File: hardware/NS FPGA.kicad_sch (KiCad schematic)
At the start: 0 parts

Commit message: Update KiCad schematics and add gowin_fpga symbol library
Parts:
- added U1: ~, Gowin FPGA:BGA-64_8x8_4.2x4.2mm, symbol Gowin FPGA:GW1NSR-4C_MG64P

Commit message: Update schematic
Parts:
- added J1: USB_C_Receptacle_USB2.0_14P, symbol Connector:USB_C_Receptacle_USB2.0_14P
- added J2, J3: Conn_01x24_Pin, symbol Connector:Conn_01x24_Pin
- added J4: Conn_01x06_Pin, symbol Connector:Conn_01x06_Pin
- added SW1: SW_Push, symbol Switch:SW_Push
- added U2: CP2102N-Axx-xQFN24, Package_DFN_QFN:QFN-24-1EP_4x4mm_P0.5mm_EP2.6x2.6mm, symbol Interface_USB:CP2102N-Axx-xQFN24
- added U3: AP2112K-3.3, Package_TO_SOT_SMD:SOT-23-5, symbol Regulator_Linear:AP2112K-3.3
- added U4: AP2112K-1.2, Package_TO_SOT_SMD:SOT-23-5, symbol Regulator_Linear:AP2112K-1.2
- added Y1: SG-8002CE, Oscillator:Oscillator_SMD_SeikoEpson_SG8002CE-4Pin_3.2x2.5mm, symbol Oscillator:SG-8002CE
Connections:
- new net: J1.A1 (GND), J1.A12 (GND), J1.B1 (GND), J1.B12 (GND)
- new net: J1.A4 (VBUS), J1.A9 (VBUS), J1.B4 (VBUS), J1.B9 (VBUS)
- new net: U2.2 (GND), U2.25 (GND)

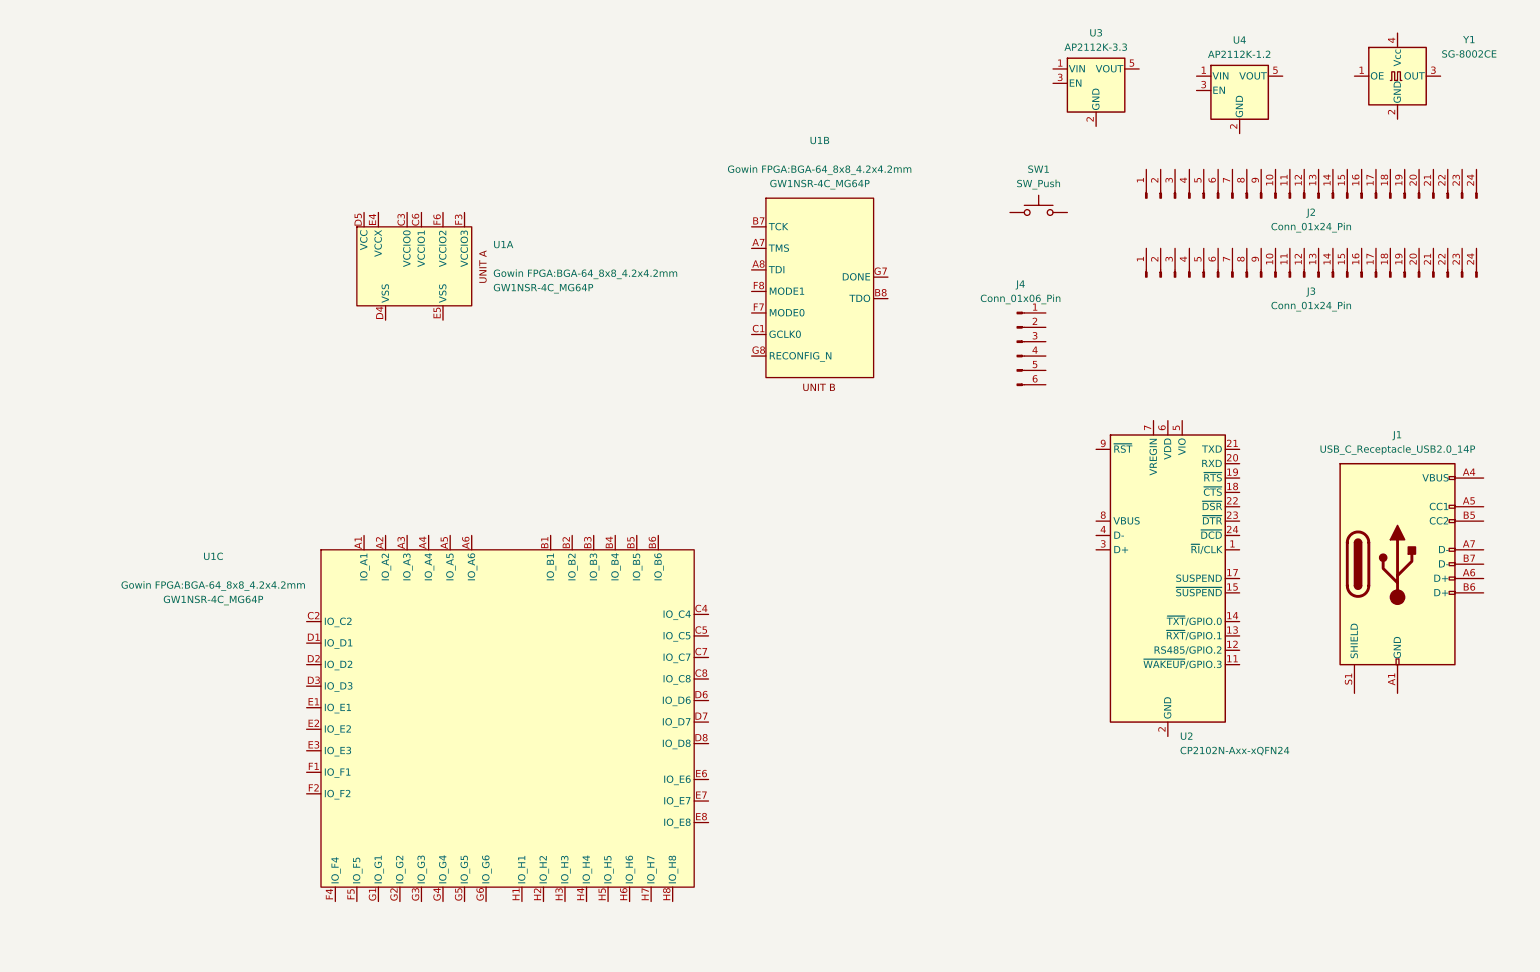
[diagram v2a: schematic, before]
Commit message: drawn 80% of the circuit schematic
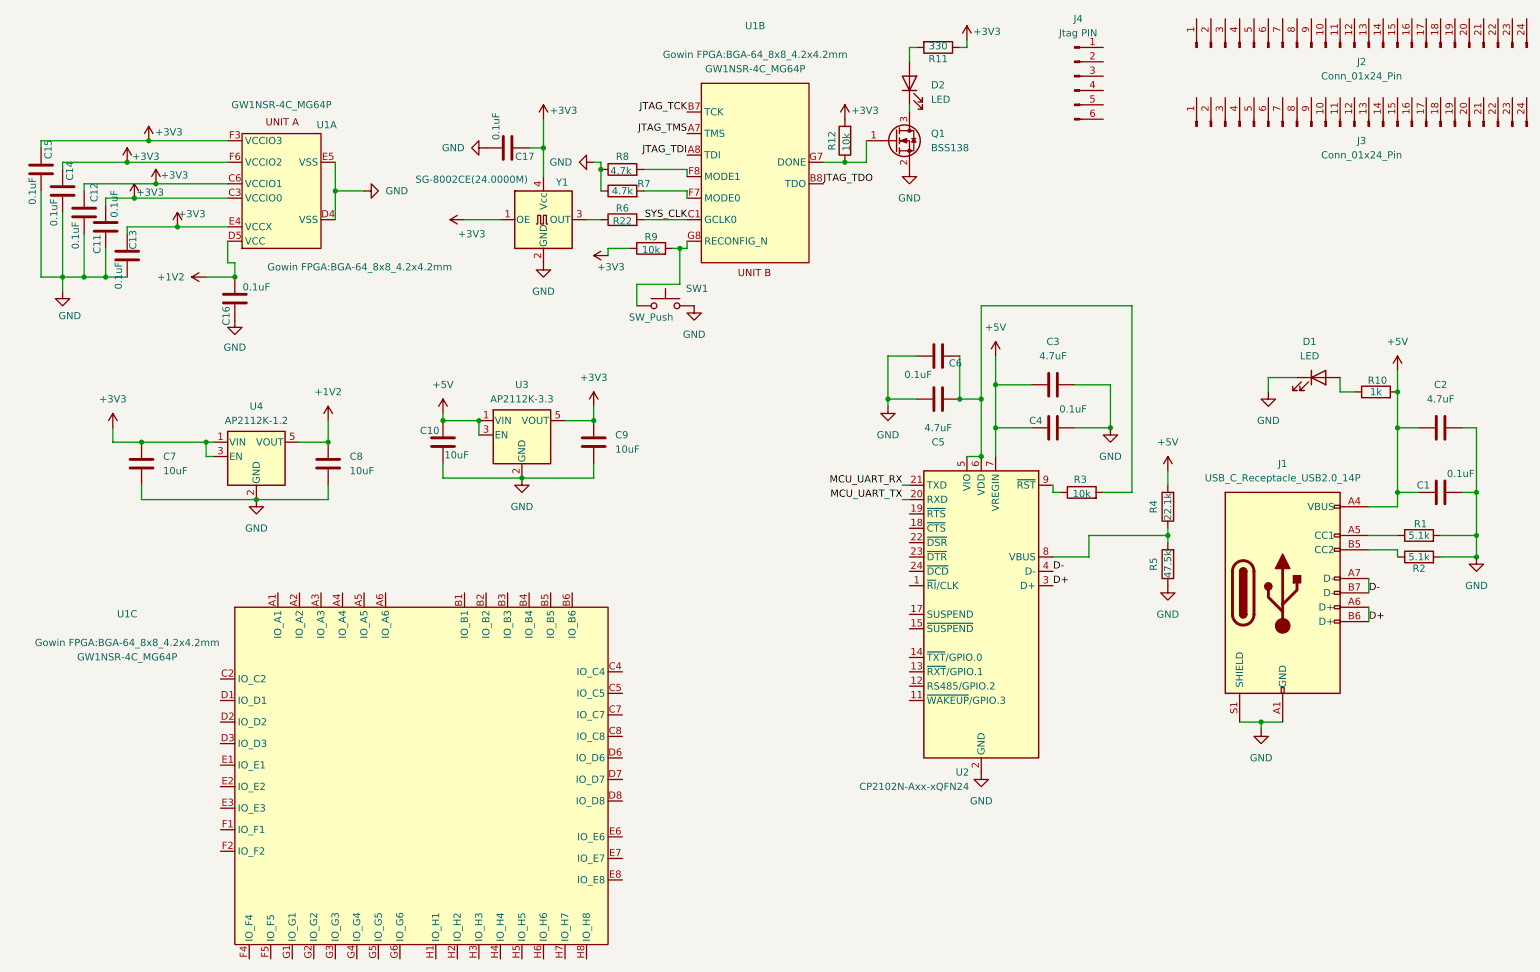
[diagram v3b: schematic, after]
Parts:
- added C1, C11, C12, C13, C14, C15, C16, C17, C4, C6: 0.1uF, symbol Device:C
- added C10, C7, C8, C9: 10uF, symbol Device:C
- added C2, C3, C5: 4.7uF, symbol Device:C
- added D1, D2: LED, symbol Device:LED
- added Q1: BSS138, Package_TO_SOT_SMD:SOT-23, symbol Transistor_FET:BSS138
- added R1, R2: 5.1k, symbol Device:R
- added R10: 1k, symbol Device:R
- added R11: 330, symbol Device:R
- added R12, R3, R9: 10k, symbol Device:R
- added R4: 22.1k, symbol Device:R
- added R5: 47.5k, symbol Device:R
- added R6: R22, symbol Device:R
- added R7, R8: 4.7k, symbol Device:R
- J4: value Conn_01x06_Pin -> Jtag PIN
- Y1: value SG-8002CE -> SG-8002CE(24.0000M)
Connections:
- net +3V3: now reaches Y1.1 (OE)
- net +3V3: now also U1.C3 (VCCIO0), U1.C6 (VCCIO1), U1.E4 (VCCX), U1.F3 (VCCIO3), U1.F6 (VCCIO2), U3.5 (VOUT), U4.1 (VIN), U4.3 (EN), Y1.4 (Vcc), C11.2, C12.1, C13.1, C14.1, C15.1, C17.1, C7.1, C9.1, R11.1, R12.2, R9.1
- net GND: now reaches Y1.2 (GND)
- net GND: now also J1.A1 (GND), J1.A12 (GND), J1.B1 (GND), J1.B12 (GND), J1.S1 (SHIELD), SW1.2, U1.D4 (VSS), U1.E5 (VSS), U2.2 (GND), U2.25 (GND), U3.2 (GND), U4.2 (GND), C1.2, C10.2, C11.1, C12.2, C13.2, C14.2, C15.2, C16.1, C17.2, C2.2, C3.2, C4.2, C5.2, C6.2, C7.2, C8.2, C9.2, D1.1 (K), Q1.2 (S), R1.2, R2.2, R5.1, R7.1, R8.1
- net at Y1.3 (OUT): now also R6.1
- net +1V2: now reaches U1.D5 (VCC)
- net +1V2: now also U4.5 (VOUT), C16.2, C8.1
- net JTAG_TMS: now reaches U1.A7 (TMS)
- net JTAG_TDI: now reaches U1.A8 (TDI)
- net JTAG_TCK: now reaches U1.B7 (TCK)
- net JTAG_TDO: now reaches U1.B8 (TDO)
- net SYS_CLK: now reaches U1.C1 (GCLK0)
- net SYS_CLK: now also R6.2
- net at U1.F7 (MODE0): now also R7.2
- net at U1.F8 (MODE1): now also R8.2
- net at U1.G7 (DONE): now also Q1.1 (G), R12.1
- net at U1.G8 (RECONFIG_N): now also SW1.1, R9.2
- net +5V: now reaches U3.1 (VIN)
- net +5V: now also J1.A4 (VBUS), J1.A9 (VBUS), J1.B4 (VBUS), J1.B9 (VBUS), U2.7 (VREGIN), U3.3 (EN), C1.1, C10.1, C2.1, C3.1, C4.1, R10.2, R4.2
- net at J1.A5 (CC1): now also R1.1
- net D+: now reaches J1.A6 (D+)
- net D+: now also J1.B6 (D+), U2.3 (D+)
- net D-: now reaches J1.A7 (D-)
- net D-: now also J1.B7 (D-), U2.4 (D-)
- net at J1.B5 (CC2): now also R2.1
- net MCU_UART_TX: now reaches U2.20 (RXD)
- net MCU_UART_RX: now reaches U2.21 (TXD)
- net at U2.5 (VIO): now also U2.6 (VDD), C5.1, C6.1, R3.2
- net at U2.8 (VBUS): now also R4.1, R5.2
- net at U2.9 (~{RST}): now also R3.1
- new net: D1.2 (A), R10.1
- new net: D2.1 (K), Q1.3 (D)
- new net: D2.2 (A), R11.2
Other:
- moved on the sheet: J1, J2, J3, J4, SW1, U1A, U1B, U1C, U2, U3, U4, Y1

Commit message: push
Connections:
- net +3V3: now also J4.1 (Pin_1)
- net GND: now also J4.6 (Pin_6)
- net JTAG_TCK: now also J4.2 (Pin_2)
- net JTAG_TDI: now also J4.4 (Pin_4)
- net JTAG_TDO: now also J4.3 (Pin_3)
- net JTAG_TMS: now also J4.5 (Pin_5)
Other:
- note added: "NS FPGA"
- moved on the sheet: C1, C10, C11, C12, C13, C14, C15, C16, C17, C2, C3, C4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

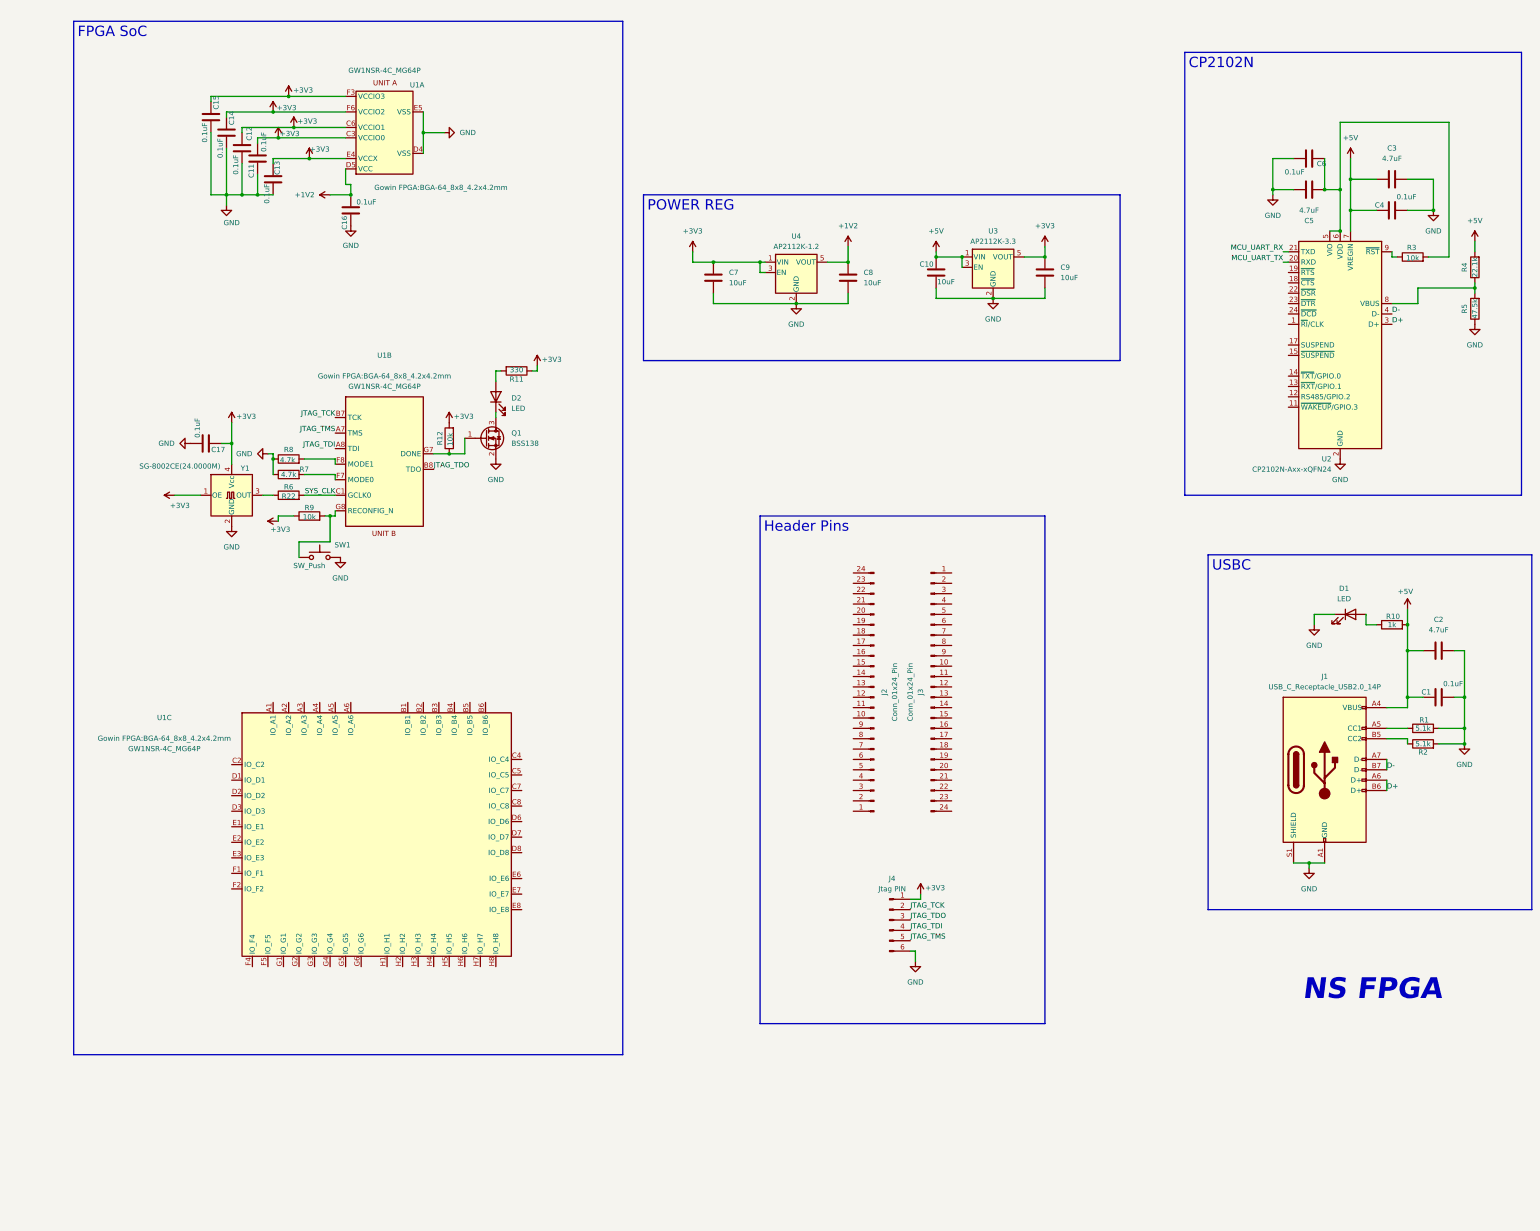
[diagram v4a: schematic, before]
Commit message: completed the schematic
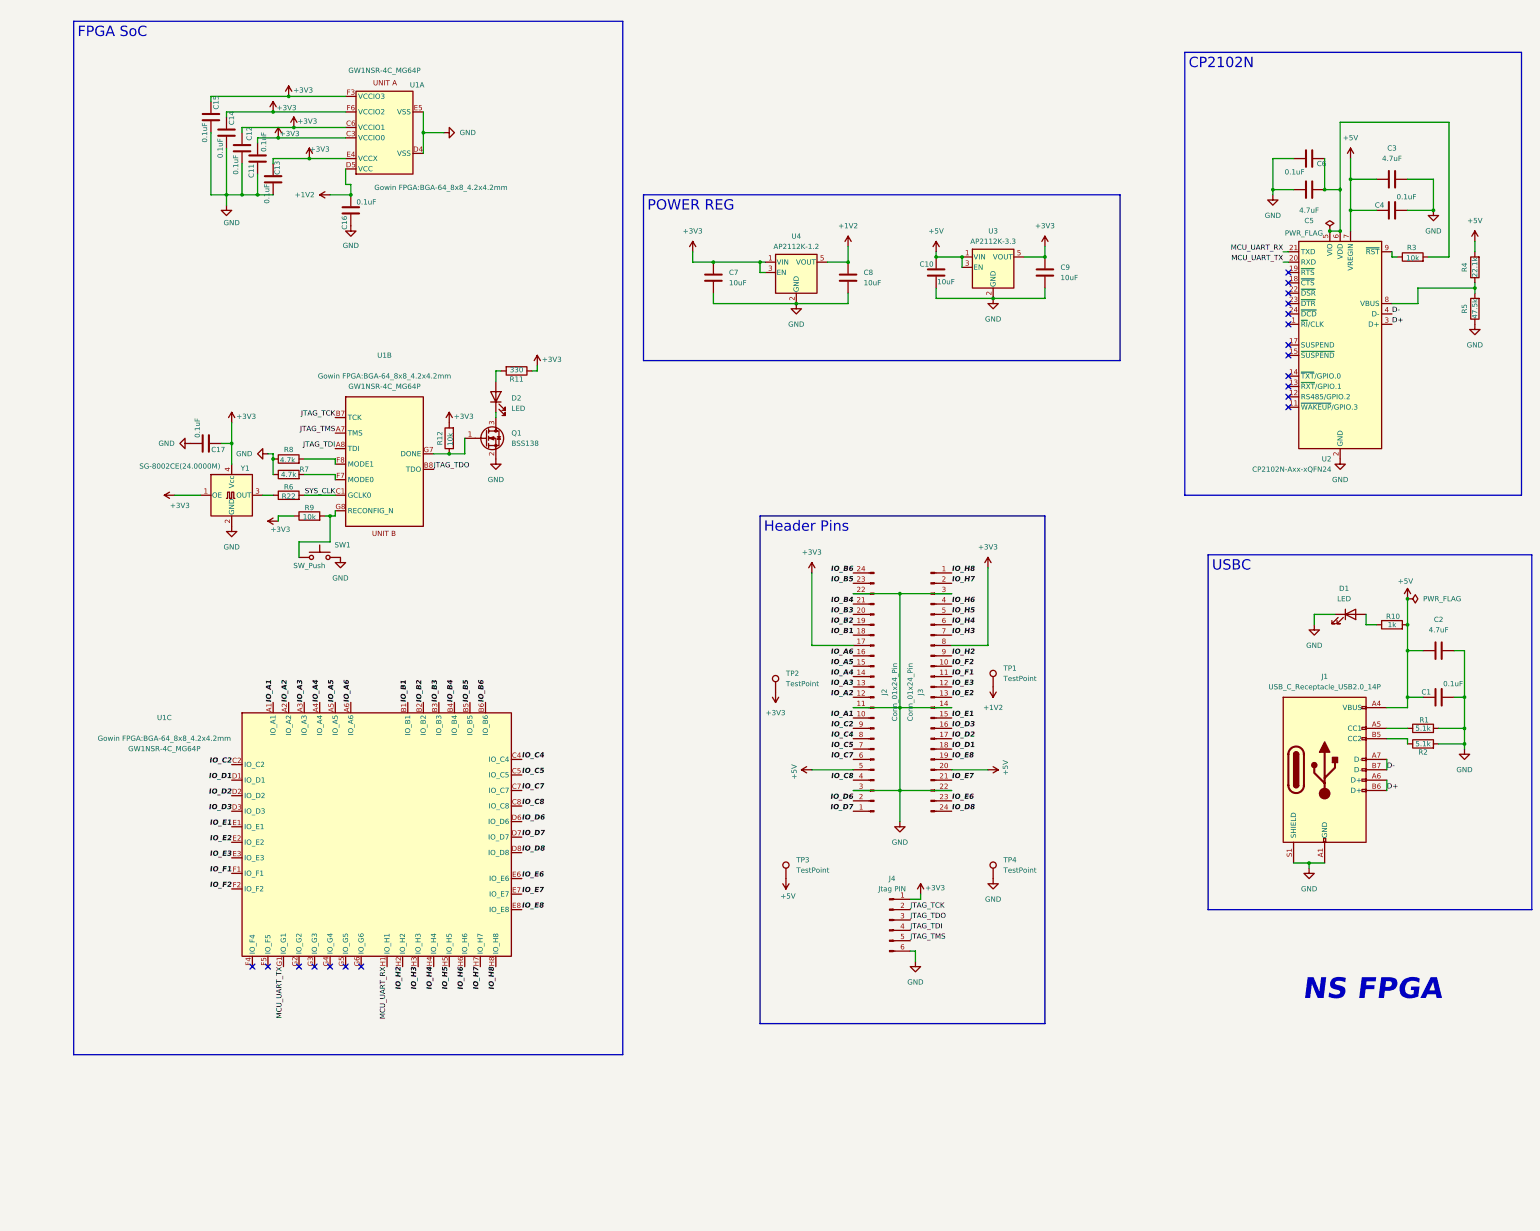
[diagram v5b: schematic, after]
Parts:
- added TP1, TP2, TP3, TP4: TestPoint, symbol Connector:TestPoint
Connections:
- net +1V2: now also TP1.1
- net +3V3: now also J2.17 (Pin_17), J3.8 (Pin_8), TP2.1
- net +5V: now also J2.5 (Pin_5), J3.20 (Pin_20), TP3.1
- net GND: now also J2.11 (Pin_11), J2.22 (Pin_22), J2.3 (Pin_3), J3.14 (Pin_14), J3.22 (Pin_22), J3.3 (Pin_3), TP4.1
- net MCU_UART_RX: now also U1.H1 (IO_H1)
- net MCU_UART_TX: now also U1.G1 (IO_G1)
- net IO_H8: now reaches J3.1 (Pin_1)
- net IO_H8: now also U1.H8 (IO_H8)
- net IO_F2: now reaches J3.10 (Pin_10)
- net IO_F2: now also U1.F2 (IO_F2)
- net IO_F1: now reaches J3.11 (Pin_11)
- net IO_F1: now also U1.F1 (IO_F1)
- net IO_E3: now reaches J3.12 (Pin_12)
- net IO_E3: now also U1.E3 (IO_E3)
- net IO_E2: now reaches J3.13 (Pin_13)
- net IO_E2: now also U1.E2 (IO_E2)
- net IO_E1: now reaches J3.15 (Pin_15)
- net IO_E1: now also U1.E1 (IO_E1)
- net IO_D3: now reaches J3.16 (Pin_16)
- net IO_D3: now also U1.D3 (IO_D3)
- net IO_D2: now reaches J3.17 (Pin_17)
- net IO_D2: now also U1.D2 (IO_D2)
- net IO_D1: now reaches J3.18 (Pin_18)
- net IO_D1: now also U1.D1 (IO_D1)
- net IO_E8: now reaches J3.19 (Pin_19)
- net IO_E8: now also U1.E8 (IO_E8)
- net IO_H7: now reaches J3.2 (Pin_2)
- net IO_H7: now also U1.H7 (IO_H7)
- net IO_E7: now reaches J3.21 (Pin_21)
- net IO_E7: now also U1.E7 (IO_E7)
- net IO_E6: now reaches J3.23 (Pin_23)
- net IO_E6: now also U1.E6 (IO_E6)
- net IO_D8: now reaches J3.24 (Pin_24)
- net IO_D8: now also U1.D8 (IO_D8)
- net IO_H6: now reaches J3.4 (Pin_4)
- net IO_H6: now also U1.H6 (IO_H6)
- net IO_H5: now reaches J3.5 (Pin_5)
- net IO_H5: now also U1.H5 (IO_H5)
- net IO_H4: now reaches J3.6 (Pin_6)
- net IO_H4: now also U1.H4 (IO_H4)
- net IO_H3: now reaches J3.7 (Pin_7)
- net IO_H3: now also U1.H3 (IO_H3)
- net IO_H2: now reaches J3.9 (Pin_9)
- net IO_H2: now also U1.H2 (IO_H2)
- net IO_D7: now reaches J2.1 (Pin_1)
- net IO_D7: now also U1.D7 (IO_D7)
- net IO_A1: now reaches J2.10 (Pin_10)
- net IO_A1: now also U1.A1 (IO_A1)
- net IO_A2: now reaches J2.12 (Pin_12)
- net IO_A2: now also U1.A2 (IO_A2)
- net IO_A3: now reaches J2.13 (Pin_13)
- net IO_A3: now also U1.A3 (IO_A3)
- net IO_A4: now reaches J2.14 (Pin_14)
- net IO_A4: now also U1.A4 (IO_A4)
- net IO_A5: now reaches J2.15 (Pin_15)
- net IO_A5: now also U1.A5 (IO_A5)
- net IO_A6: now reaches J2.16 (Pin_16)
- net IO_A6: now also U1.A6 (IO_A6)
- net IO_B1: now reaches J2.18 (Pin_18)
- net IO_B1: now also U1.B1 (IO_B1)
- net IO_B2: now reaches J2.19 (Pin_19)
- net IO_B2: now also U1.B2 (IO_B2)
- net IO_D6: now reaches J2.2 (Pin_2)
- net IO_D6: now also U1.D6 (IO_D6)
- net IO_B3: now reaches J2.20 (Pin_20)
- net IO_B3: now also U1.B3 (IO_B3)
- net IO_B4: now reaches J2.21 (Pin_21)
- net IO_B4: now also U1.B4 (IO_B4)
- net IO_B5: now reaches J2.23 (Pin_23)
- net IO_B5: now also U1.B5 (IO_B5)
- net IO_B6: now reaches J2.24 (Pin_24)
- net IO_B6: now also U1.B6 (IO_B6)
- net IO_C8: now reaches J2.4 (Pin_4)
- net IO_C8: now also U1.C8 (IO_C8)
- net IO_C7: now reaches J2.6 (Pin_6)
- net IO_C7: now also U1.C7 (IO_C7)
- net IO_C5: now reaches J2.7 (Pin_7)
- net IO_C5: now also U1.C5 (IO_C5)
- net IO_C4: now reaches J2.8 (Pin_8)
- net IO_C4: now also U1.C4 (IO_C4)
- net IO_C2: now reaches J2.9 (Pin_9)
- net IO_C2: now also U1.C2 (IO_C2)
- no-connect marks 0 -> 19

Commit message: routed some of the BGA chip
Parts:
- C1, C10, C2, C3, C4, C5, C6, C7, C8, C9: footprint (none) -> Capacitor_SMD:C_0402_1005Metric
- C11, C12, C13, C14, C15, C16, C17: footprint (none) -> Capacitor_SMD:C_0201_0603Metric
- D1, D2: footprint (none) -> LED_SMD:LED_0201_0603Metric
- J1: footprint (none) -> Connector_USB:USB_C_Receptacle_HCTL_HC-TYPE-C-16P-01A
- J2, J3: footprint (none) -> Connector_PinHeader_2.54mm:PinHeader_1x24_P2.54mm_Vertical
- J4: footprint (none) -> Connector_PinHeader_2.54mm:PinHeader_1x06_P2.54mm_Vertical
- R1, R12, R2, R3, R9: footprint (none) -> Resistor_SMD:R_0402_1005Metric
- R10, R11, R4, R5, R6, R7, R8: footprint (none) -> Resistor_SMD:R_0201_0603Metric
- SW1: footprint (none) -> Button_Switch_SMD:SW_SPST_EVQP2_ShortPushTravel_H2.1mm
- TP1, TP2, TP3, TP4: footprint (none) -> TestPoint:TestPoint_Pad_D1.0mm
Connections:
- net IO_D3: no longer J3.16 (Pin_16)
- net IO_D6: no longer U1.D6 (IO_D6)
- net IO_G3: now reaches U1.G3 (IO_G3)
- net IO_G3: now also J3.23 (Pin_23)
- net IO_G4: now reaches U1.G4 (IO_G4)
- net IO_G4: now also J3.21 (Pin_21)
- net IO_G5: now reaches U1.G5 (IO_G5)
- net IO_G5: now also J3.16 (Pin_16)
- net IO_D2: no longer names the net of J3.17 (Pin_17)
- net IO_D2: no longer U1.D2 (IO_D2)
- net IO_E2: no longer names the net of J3.13 (Pin_13)
- net IO_E2: no longer U1.E2 (IO_E2)
- net IO_E3: no longer names the net of J3.12 (Pin_12)
- net IO_E3: no longer U1.E3 (IO_E3)
- net IO_E6: no longer names the net of U1.E6 (IO_E6)
- net IO_E6: no longer J3.23 (Pin_23)
- net IO_E7: no longer names the net of U1.E7 (IO_E7)
- net IO_E7: no longer J3.21 (Pin_21)
- net IO_F2: no longer names the net of J3.10 (Pin_10)
- net IO_F2: no longer U1.F2 (IO_F2)
- no-connect marks 19 -> 25
